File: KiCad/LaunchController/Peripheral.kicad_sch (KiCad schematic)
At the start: 8 parts, among them J11 RJ45, J15 CONN_AUDIO, J16 CONN_SPEAKER, U2 24LC256, U6 DFPlayer, U7 LTC485CN8#PBF

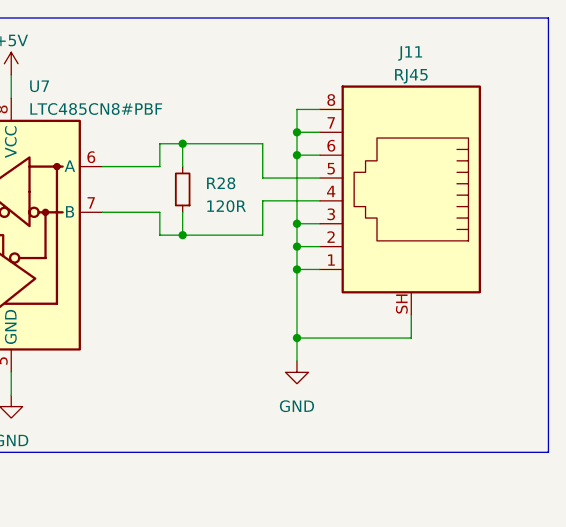
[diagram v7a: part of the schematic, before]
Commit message: RS485をモジュラージャックからプッシュインコネクタに変更
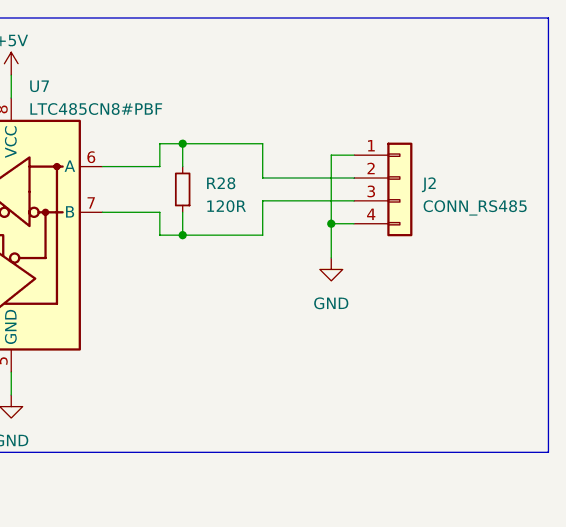
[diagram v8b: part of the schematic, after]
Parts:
- removed J11: RJ45, TSRP_Connector_Hirose:TM11R-5M2-88, symbol Connector:RJ45_Shielded
- added J2: CONN_RS485, TSRP_TerminalBlock_Alphaplus:TB401-1-4-E, symbol Connector_Generic:Conn_01x04
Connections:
- net GND: now also J2.1 (Pin_1), J2.4 (Pin_4)
- net at R28.1, U7.7 (B): now also J2.3 (Pin_3)
- net at R28.2, U7.6 (A): now also J2.2 (Pin_2)
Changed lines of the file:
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@@
 (kicad_sch (version 20230121) (generator eeschema)
   (paper "A4")
-  (junction (at 196.85 48.26) (diameter 0) (color 0 0 0 0)
-  )
   (junction (at 17.78 29.21) (diameter 0) (color 0 0 0 0)
   )
-  (junction (at 196.85 25.4) (diameter 0) (color 0 0 0 0)
-  )
-  (junction (at 196.85 40.64) (diameter 0) (color 0 0 0 0)
-  )
   (junction (at 184.15 26.67) (diameter 0) (color 0 0 0 0)
   )
-  (junction (at 196.85 27.94) (diameter 0) (color 0 0 0 0)
-  )
   (junction (at 152.4 36.83) (diameter 0) (color 0 0 0 0)
   )
-  (junction (at 196.85 38.1) (diameter 0) (color 0 0 0 0)
-  )
   (junction (at 184.15 36.83) (diameter 0) (color 0 0 0 0)
   )
+  (junction (at 200.66 35.56) (diameter 0) (color 0 0 0 0)
+  )
   (junction (at 111.76 57.15) (diameter 0) (color 0 0 0 0)
   )
@@
   )
   (junction (at 17.78 31.75) (diameter 0) (color 0 0 0 0)
-  )
-  (junction (at 196.85 35.56) (diameter 0) (color 0 0 0 0)
   )
   (no_connect (at 124.46 48.26))
@@
     (stroke (width 0) (type default))
   )
-  (wire (pts (xy 199.39 33.02) (xy 193.04 33.02))
-    (stroke (width 0) (type default))
-  )
   (wire (pts (xy 175.26 34.29) (xy 181.61 34.29))
     (stroke (width 0) (type default))
@@
     (stroke (width 0) (type default))
   )
-  (wire (pts (xy 196.85 38.1) (xy 196.85 40.64))
-    (stroke (width 0) (type default))
-  )
   (wire (pts (xy 184.15 26.67) (xy 184.15 29.21))
     (stroke (width 0) (type default))
   )
+  (wire (pts (xy 200.66 35.56) (xy 203.2 35.56))
+    (stroke (width 0) (type default))
+  )
   (wire (pts (xy 17.78 39.37) (xy 30.48 39.37))
     (stroke (width 0) (type default))
@@
     (stroke (width 0) (type default))
   )
-  (wire (pts (xy 196.85 35.56) (xy 199.39 35.56))
-    (stroke (width 0) (type default))
-  )
-  (wire (pts (xy 193.04 30.48) (xy 199.39 30.48))
+  (wire (pts (xy 203.2 27.94) (xy 200.66 27.94))
+    (stroke (width 0) (type default))
+  )
+  (wire (pts (xy 193.04 33.02) (xy 203.2 33.02))
     (stroke (width 0) (type default))
   )
@@
     (stroke (width 0) (type default))
   )
-  (wire (pts (xy 196.85 27.94) (xy 196.85 35.56))
-    (stroke (width 0) (type default))
-  )
   (wire (pts (xy 17.78 26.67) (xy 17.78 29.21))
     (stroke (width 0) (type default))
@@
     (stroke (width 0) (type default))
   )
-  (wire (pts (xy 196.85 25.4) (xy 199.39 25.4))
-    (stroke (width 0) (type default))
-  )
   (wire (pts (xy 181.61 36.83) (xy 184.15 36.83))
     (stroke (width 0) (type default))
   )
-  (wire (pts (xy 196.85 38.1) (xy 199.39 38.1))
-    (stroke (width 0) (type default))
-  )
-  (wire (pts (xy 196.85 35.56) (xy 196.85 38.1))
-    (stroke (width 0) (type default))
-  )
   (wire (pts (xy 40.64 29.21) (xy 43.18 29.21))
     (stroke (width 0) (type default))
@@
     (stroke (width 0) (type default))
   )
+  (wire (pts (xy 200.66 27.94) (xy 200.66 35.56))
+    (stroke (width 0) (type default))
+  )
   (wire (pts (xy 181.61 29.21) (xy 181.61 26.67))
     (stroke (width 0) (type default))
   )
-  (wire (pts (xy 196.85 22.86) (xy 196.85 25.4))
-    (stroke (width 0) (type default))
-  )
   (wire (pts (xy 30.48 19.05) (xy 30.48 21.59))
     (stroke (width 0) (type default))
@@
     (stroke (width 0) (type default))
   )
-  (wire (pts (xy 196.85 40.64) (xy 196.85 48.26))
-    (stroke (width 0) (type default))
-  )
-  (wire (pts (xy 196.85 48.26) (xy 196.85 50.8))
-    (stroke (width 0) (type default))
-  )
   (wire (pts (xy 154.94 34.29) (xy 152.4 34.29))
     (stroke (width 0) (type default))
@@
     (stroke (width 0) (type default))
   )
-  (wire (pts (xy 209.55 45.72) (xy 209.55 48.26))
-    (stroke (width 0) (type default))
-  )
   (wire (pts (xy 152.4 31.75) (xy 154.94 31.75))
     (stroke (width 0) (type default))
@@
     (stroke (width 0) (type default))
   )
+  (wire (pts (xy 193.04 30.48) (xy 203.2 30.48))
+    (stroke (width 0) (type default))
+  )
   (wire (pts (xy 193.04 33.02) (xy 193.04 36.83))
     (stroke (width 0) (type default))
   )
-  (wire (pts (xy 199.39 22.86) (xy 196.85 22.86))
-    (stroke (width 0) (type default))
-  )
-  (wire (pts (xy 196.85 48.26) (xy 209.55 48.26))
+  (wire (pts (xy 200.66 35.56) (xy 200.66 39.37))
     (stroke (width 0) (type default))
   )
@@
   )
   (wire (pts (xy 149.86 36.83) (xy 152.4 36.83))
-    (stroke (width 0) (type default))
-  )
-  (wire (pts (xy 196.85 25.4) (xy 196.85 27.94))
-    (stroke (width 0) (type default))
-  )
-  (wire (pts (xy 196.85 40.64) (xy 199.39 40.64))
-    (stroke (width 0) (type default))
-  )
-  (wire (pts (xy 196.85 27.94) (xy 199.39 27.94))
     (stroke (width 0) (type default))
   )
@@
     )
   )
-  (symbol (lib_id "power:GND") (at 196.85 50.8 0) (unit 1)
-    (in_bom yes) (on_board yes) (dnp no) (fields_autoplaced)
-    (property "Reference" "#PWR051" (at 196.85 57.15 0)
-      (effects (font (size 1.27 1.27)) hide)
-    )
-    (property "Value" "GND" (at 196.85 55.88 0)
-      (effects (font (size 1.27 1.27)))
-    )
-    (property "Footprint" "" (at 196.85 50.8 0)
-      (effects (font (size 1.27 1.27)) hide)
-    )
-    (property "Datasheet" "" (at 196.85 50.8 0)
+  (symbol (lib_id "power:GND") (at 200.66 39.37 0) (unit 1)
+    (in_bom yes) (on_board yes) (dnp no) (fields_autoplaced)
+    (property "Reference" "#PWR051" (at 200.66 45.72 0)
+      (effects (font (size 1.27 1.27)) hide)
+    )
+    (property "Value" "GND" (at 200.66 44.45 0)
+      (effects (font (size 1.27 1.27)))
+    )
+    (property "Footprint" "" (at 200.66 39.37 0)
+      (effects (font (size 1.27 1.27)) hide)
+    )
+    (property "Datasheet" "" (at 200.66 39.37 0)
       (effects (font (size 1.27 1.27)) hide)
     )
@@
         (path "/628d040b-43bf-4733-804f-091644a90124/092bb5f6-479a-4342-8285-14bd550a4a8c"
           (reference "#PWR054") (unit 1)
+        )
+      )
+    )
+  )
+  (symbol (lib_id "Connector_Generic:Conn_01x04") (at 208.28 30.48 0) (unit 1)
+    (in_bom yes) (on_board yes) (dnp no) (fields_autoplaced)
+    (property "Reference" "J2" (at 210.82 31.115 0)
+      (effects (font (size 1.27 1.27)) (justify left))
+    )
+    (property "Value" "CONN_RS485" (at 210.82 33.655 0)
+      (effects (font (size 1.27 1.27)) (justify left))
+    )
+    (property "Footprint" "TSRP_TerminalBlock_Alphaplus:TB401-1-4-E" (at 208.28 30.48 0)
+      (effects (font (size 1.27 1.27)) hide)
+    )
+    (property "Datasheet" "https://akizukidenshi.com/catalog/g/gP-07756/" (at 208.28 30.48 0)
+      (effects (font (size 1.27 1.27)) hide)
+    )
+    (property "LCSC" "" (at 208.28 30.48 0)
+      (effects (font (size 1.27 1.27)) hide)
+    )
+    (pin "1")
+    (pin "2")
+    (pin "3")
+    (pin "4")
+    (instances
+      (project "LaunchController"
+        (path "/628d040b-43bf-4733-804f-091644a90124"
+          (reference "J2") (unit 1)
+        )
+        (path "/628d040b-43bf-4733-804f-091644a90124/092bb5f6-479a-4342-8285-14bd550a4a8c"
+          (reference "J15") (unit 1)
         )
       )
@@
         )
       )
-    )
-  )
-  (symbol (lib_id "Connector:RJ45_Shielded") (at 209.55 33.02 0) (mirror y) (unit 1)
-    (in_bom yes) (on_board yes) (dnp no)
-    (property "Reference" "J11" (at 209.55 16.51 0)
-      (effects (font (size 1.27 1.27)))
-    )
-    (property "Value" "RJ45" (at 209.55 19.05 0)
-      (effects (font (size 1.27 1.27)))
-    )
-    (property "Footprint" "TSRP_Connector_Hirose:TM11R-5M2-88" (at 209.55 32.385 90)
-      (effects (font (size 1.27 1.27)) hide)
-    )
-    (property "Datasheet" "https://www.monotaro.com/p/4743/2638/" (at 209.55 32.385 90)
-      (effects (font (size 1.27 1.27)) hide)
-    )
-    (property "LCSC" "" (at 209.55 33.02 0)
-      (effects (font (size 1.27 1.27)) hide)
-    )
-    (pin "1")
-    (pin "2")
-    (pin "3")
-    (pin "4")
-    (pin "5")
-    (pin "6")
-    (pin "7")
-    (pin "8")
-    (pin "SH")
-    (instances
-      (project "LaunchController"
-        (path "/628d040b-43bf-4733-804f-091644a90124/092bb5f6-479a-4342-8285-14bd550a4a8c"
-          (reference "J11") (unit 1)
-        )
-      )
